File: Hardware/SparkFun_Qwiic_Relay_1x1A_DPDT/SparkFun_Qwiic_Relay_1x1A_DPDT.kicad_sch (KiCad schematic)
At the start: 38 parts, among them J1 Qwiic_RA, J2 Conn_01x03, J3 Qwiic_RA, J4 Conn_01x01, J5 I2C, J6 3.5mm, K2 G6K-2F-Y DC3, Q2 LMUN2235LT1G, U2 TCA9555RTWR, U3 EL3H7

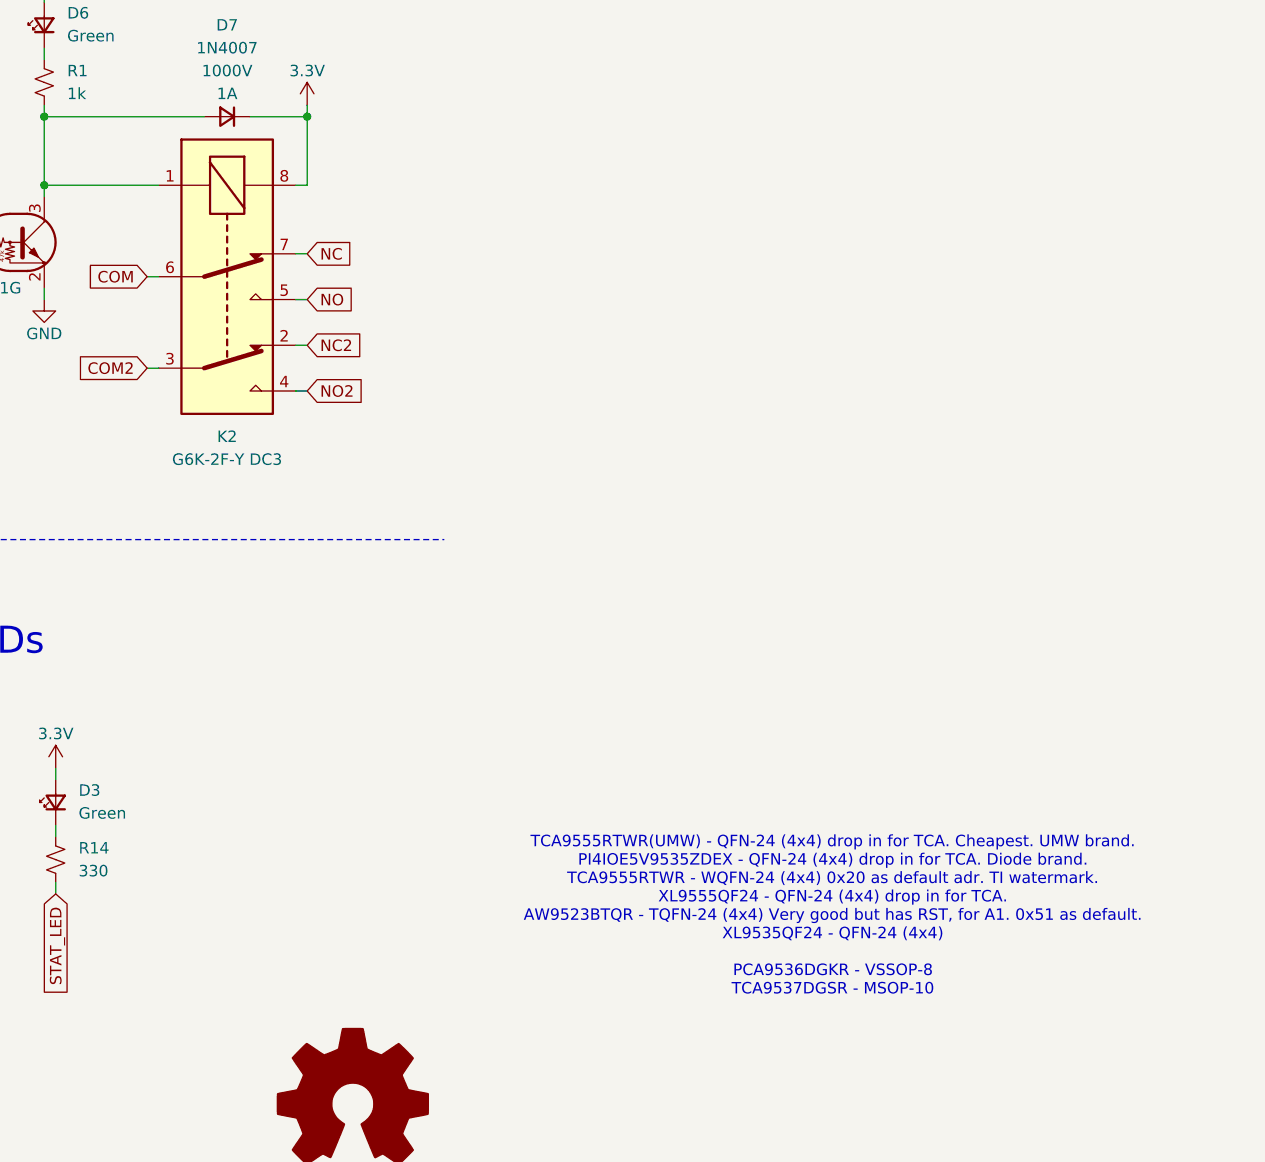
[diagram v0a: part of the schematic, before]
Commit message: Fix polarized relay. Increase version on PCB and SCH.
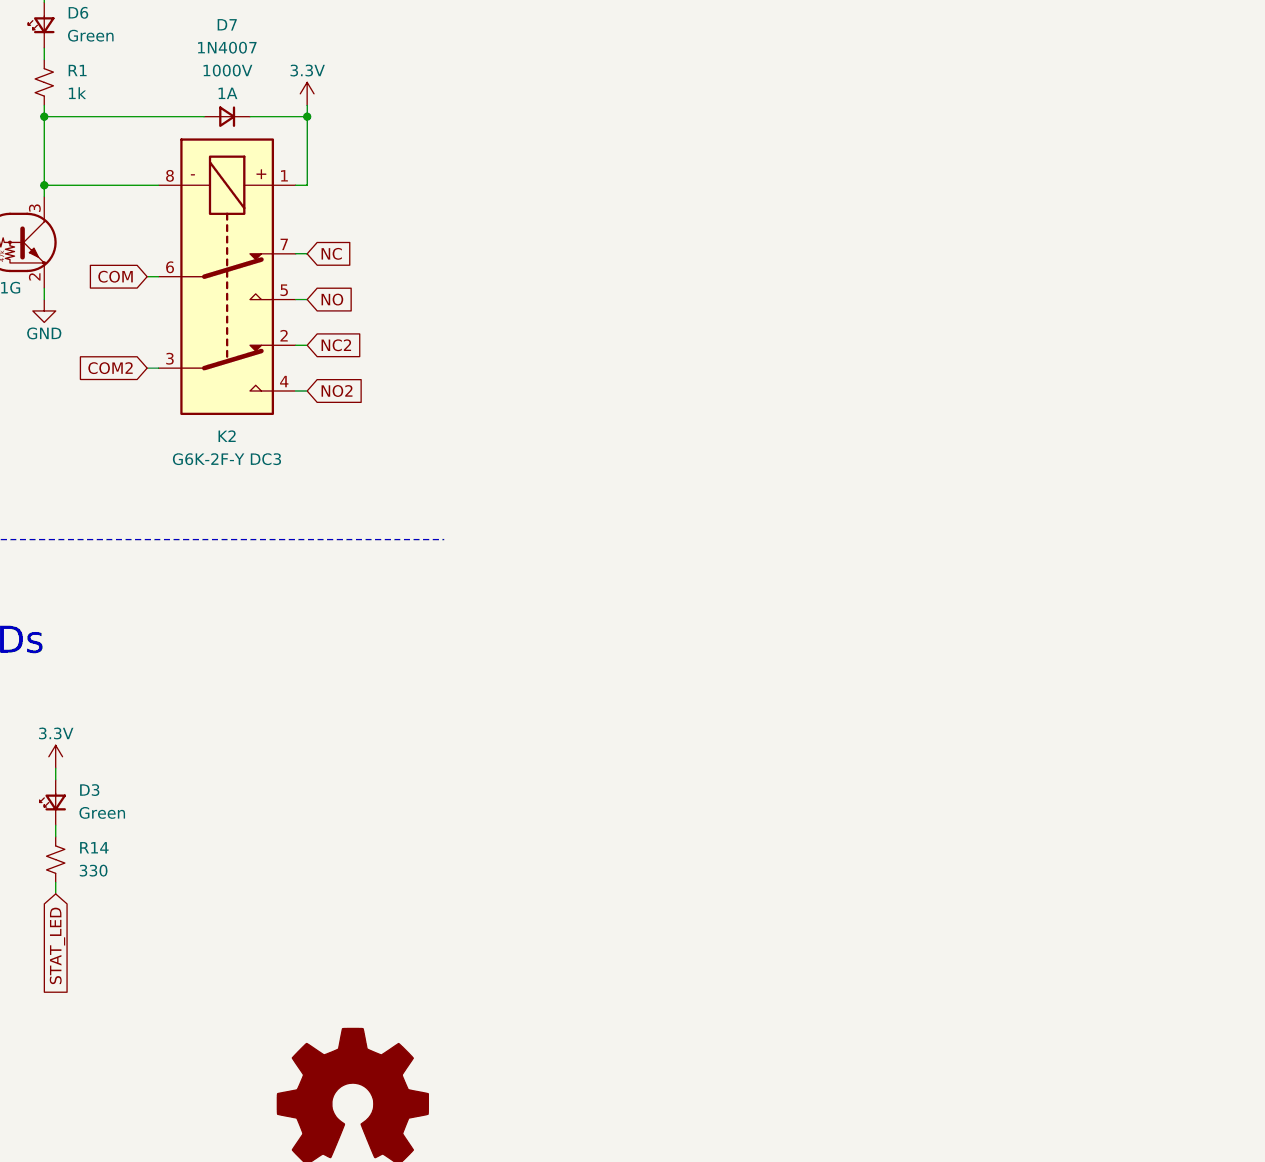
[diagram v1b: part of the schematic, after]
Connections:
- net 3.3V: now also K2.1; no longer K2.8
- net at D7.2 (A), Q2.3 (C), R1.1: now also K2.8; no longer K2.1
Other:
- note removed: "TCA9555RTWR(UMW) - QFN-24 (4x4) drop in for TCA. Cheapest. UMW brand. PI4IOE5V9535ZDEX - QFN-24 (4x4) drop in for TCA. Diode brand. TCA9555RTWR - WQFN-24 (4x4) 0x20 as default adr. TI watermark. XL9555QF24 - QFN-24 (4x4) drop in for TCA. AW9523BTQR - TQFN-24 (4x4) Very good but has RST, for A1. 0x51 as default. XL9535QF24 - QFN-24 (4x4) PCA9536DGKR - VSSOP-8 TCA9537DGSR - MSOP-10"
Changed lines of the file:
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@@
 		(title "SparkFun Qwiic Relay 1x1A DPDT")
 		(date "2025-12-08")
-		(rev "v10")
+		(rev "v11")
 		(comment 1 "Designed by: N. Seidle")
 	)
-	(text "TCA9555RTWR(UMW) - QFN-24 (4x4) drop in for TCA. Cheapest. UMW brand.\nPI4IOE5V9535ZDEX - QFN-24 (4x4) drop in for TCA. Diode brand.\nTCA9555RTWR - WQFN-24 (4x4) 0x20 as default adr. TI watermark.\nXL9555QF24 - QFN-24 (4x4) drop in for TCA. \nAW9523BTQR - TQFN-24 (4x4) Very good but has RST, for A1. 0x51 as default.\nXL9535QF24 - QFN-24 (4x4)\n\nPCA9536DGKR - VSSOP-8\nTCA9537DGSR - MSOP-10\n"
-		(exclude_from_sim no)
-		(at 309.88 135.89 0)
-		(effects
-			(font
-				(size 1.27 1.27)
-			)
-		)
-	)
 	(text "Internal Default 100k Pullup Resistors on all GPIO"
